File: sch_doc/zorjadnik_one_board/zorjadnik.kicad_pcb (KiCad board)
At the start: 2 copper layers, 63 parts, among them J1 OUT1, J10 output GND, J11 power supply GND, J12 spare port, J2 OUT2, J3 Vsb, J4 GND, J6 firmware, J7 cooling fan, J9 power supply Vout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

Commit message: собрал
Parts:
- moved R3 0.98 mm to (92.1, 46.1)
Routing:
- net GND: track 165.4 -> 167.3 mm
- net Net-(D5-Pad3): track 77.0 -> 75.7 mm
- net Net-(C7-Pad1): track 20.5 -> 21.5 mm
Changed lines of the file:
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@@
     (thickness 1.6)
     (drawings 0)
-    (tracks 480)
+    (tracks 483)
     (zones 0)
     (modules 63)
@@
   )
   (setup
-    (last_trace_width 1.5)
+    (last_trace_width 0.5)
     (user_trace_width 0.2)
     (user_trace_width 0.3)
@@
   )
   (module Resistor_SMD:R_0805_2012Metric (layer F.Cu)
-    (at 91.14536 46.14164 180)
+    (at 92.1258 46.09084 180)
     (descr "Resistor SMD 0805 (2012 Metric), square (rectangular) end terminal, IPC_7351 nominal, (Body size source: https://docs.google.com/spreadsheets/d/1BsfQQcO9C6DZCsRaXUlFlo91Tg2WpOkGARC1WS5S8t0/edit?usp=sharing), generated with kicad-footprint-generator")
     (tags resistor)
@@
     )
   )
+  (segment (start 107.07116 40.78732) (end 103.81488 40.78732) (width 0.5) (layer F.Cu) (net 1))
   (via (at 98.298 46.11624) (size 1.7) (drill 0.4) (layers F.Cu B.Cu) (net 1))
-  (segment (start 104.55148 47.91964) (end 104.55148 47.91456) (width 0.5) (layer B.Cu) (net 3))
-  (segment (start 104.55148 47.91456) (end 103.73868 47.10176) (width 0.5) (layer B.Cu) (net 3))
   (via (at 94.81566 55.36946) (size 1.7) (drill 0.4) (layers F.Cu B.Cu) (net 1))
   (segment (start 69.24358 67.9129) (end 69.22058 67.8899) (width 0.5) (layer F.Cu) (net 1))
@@
   (segment (start 78.99644 59.03468) (end 79.02956 59.00156) (width 0.5) (layer F.Cu) (net 1))
   (segment (start 79.02956 57.58698) (end 79.02448 57.5819) (width 0.5) (layer F.Cu) (net 1))
-  (segment (start 79.02956 59.00156) (end 79.02956 57.58698) (width 0.5) (layer F.Cu) (net 1))
   (segment (start 79.02956 59.00156) (end 80.129601 59.00156) (width 0.4) (layer F.Cu) (net 1))
   (segment (start 81.407561 59.364559) (end 82.057561 60.014559) (width 0.4) (layer F.Cu) (net 1))
@@
   (segment (start 107.25912 53.7778) (end 107.25912 54.06644) (width 0.5) (layer B.Cu) (net 2))
   (segment (start 107.54152 53.4954) (end 107.25912 53.7778) (width 0.5) (layer B.Cu) (net 2))
+  (segment (start 104.55148 47.91964) (end 104.55148 47.91456) (width 0.5) (layer B.Cu) (net 3))
+  (segment (start 104.55148 47.91456) (end 103.73868 47.10176) (width 0.5) (layer B.Cu) (net 3))
   (segment (start 104.50068 33.80232) (end 106.75112 33.80232) (width 0.3) (layer B.Cu) (net 3))
   (segment (start 104.12476 40.78732) (end 106.74096 40.78732) (width 0.5) (layer B.Cu) (net 3))
@@
   (segment (start 105.47604 44.391566) (end 105.361726 44.50588) (width 1.5) (layer F.Cu) (net 23))
   (segment (start 105.47604 42.6238) (end 105.47604 44.391566) (width 1.5) (layer F.Cu) (net 23))
-  (segment (start 92.26244 45.96206) (end 92.08286 46.14164) (width 0.5) (layer F.Cu) (net 23))
   (segment (start 73.52284 43.68692) (end 74.037 44.20108) (width 1.5) (layer F.Cu) (net 23))
   (segment (start 73.52284 43.01192) (end 73.52284 43.68692) (width 1.5) (layer F.Cu) (net 23))
   (segment (start 103.89876 44.20108) (end 104.089246 44.391566) (width 1.5) (layer F.Cu) (net 23))
   (segment (start 104.089246 44.391566) (end 105.47604 44.391566) (width 1.5) (layer F.Cu) (net 23))
-  (segment (start 92.08286 44.20338) (end 92.08286 46.14164) (width 0.5) (layer F.Cu) (net 23))
   (segment (start 92.08516 44.20108) (end 92.08286 44.20338) (width 0.5) (layer F.Cu) (net 23))
   (segment (start 74.037 44.20108) (end 92.08516 44.20108) (width 1.5) (layer F.Cu) (net 23))
@@
   (segment (start 95.75292 44.20108) (end 95.72244 44.23156) (width 0.5) (layer F.Cu) (net 23))
   (segment (start 95.75292 44.20108) (end 103.89876 44.20108) (width 1.5) (layer F.Cu) (net 23))
-  (segment (start 92.08516 44.20108) (end 95.75292 44.20108) (width 1.5) (layer F.Cu) (net 23))
-  (segment (start 92.30054 45.92396) (end 92.08286 46.14164) (width 0.5) (layer F.Cu) (net 23))
-  (segment (start 95.72244 45.92396) (end 92.30054 45.92396) (width 0.5) (layer F.Cu) (net 23))
+  (segment (start 95.55556 46.09084) (end 95.72244 45.92396) (width 0.5) (layer F.Cu) (net 23))
+  (segment (start 93.0633 46.09084) (end 95.55556 46.09084) (width 0.5) (layer F.Cu) (net 23))
+  (segment (start 93.0633 44.22926) (end 93.0633 46.09084) (width 0.5) (layer F.Cu) (net 23))
+  (segment (start 93.03512 44.20108) (end 93.0633 44.22926) (width 0.5) (layer F.Cu) (net 23))
+  (segment (start 93.03512 44.20108) (end 95.75292 44.20108) (width 1.5) (layer F.Cu) (net 23))
+  (segment (start 92.08516 44.20108) (end 93.03512 44.20108) (width 1.5) (layer F.Cu) (net 23))
   (segment (start 90.37856 58.67306) (end 91.89306 58.67306) (width 0.4) (layer F.Cu) (net 24) (status 10))
   (segment (start 92.04706 58.51906) (end 93.16456 58.51906) (width 0.4) (layer F.Cu) (net 24) (status 20))
@@
   (segment (start 90.20556 50.14976) (end 90.20556 49.385558) (width 0.4) (layer F.Cu) (net 24))
   (segment (start 90.20556 49.385558) (end 90.20556 48.6387) (width 0.5) (layer F.Cu) (net 24))
-  (segment (start 90.20786 48.6364) (end 90.20786 46.14164) (width 0.5) (layer F.Cu) (net 24))
   (segment (start 90.20556 48.6387) (end 90.20786 48.6364) (width 0.5) (layer F.Cu) (net 24))
   (segment (start 90.21064 54.77256) (end 90.21064 55.84952) (width 0.5) (layer F.Cu) (net 24))
@@
   (segment (start 89.08796 56.93156) (end 90.21064 55.84952) (width 0.3) (layer F.Cu) (net 24))
   (segment (start 90.21064 55.84952) (end 90.20556 55.81396) (width 0.3) (layer F.Cu) (net 24))
+  (segment (start 90.20556 48.6387) (end 90.20556 46.18736) (width 0.5) (layer F.Cu) (net 24))
+  (segment (start 90.30208 46.09084) (end 91.1883 46.09084) (width 0.5) (layer F.Cu) (net 24))
+  (segment (start 90.20556 46.18736) (end 90.30208 46.09084) (width 0.5) (layer F.Cu) (net 24))
   (segment (start 90.37856 58.02306) (end 91.40356 58.02306) (width 0.3) (layer F.Cu) (net 25) (status 10))
   (segment (start 91.765229 58.02306) (end 91.98356 57.804729) (width 0.3) (layer F.Cu) (net 25))

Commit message: полирнул меню, теперь есть функция выкючения
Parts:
- removed R14, R15: 100, Resistor_SMD:R_0805_2012Metric
- turned RV1 to 0 degrees
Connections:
- CB1 pad 2: Net-(CB1-Pad2) -> mode_but
- CB2 pad 2: Net-(CB2-Pad2) -> sel_but
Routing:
- net sel_but: track 42.6 -> 53.3 mm
- net mode_but: track 42.0 -> 52.7 mm
- net Net-(CB2-Pad2): track 8.81 -> 0.00 mm
- net Net-(CB1-Pad2): track 8.80 -> 0.00 mm

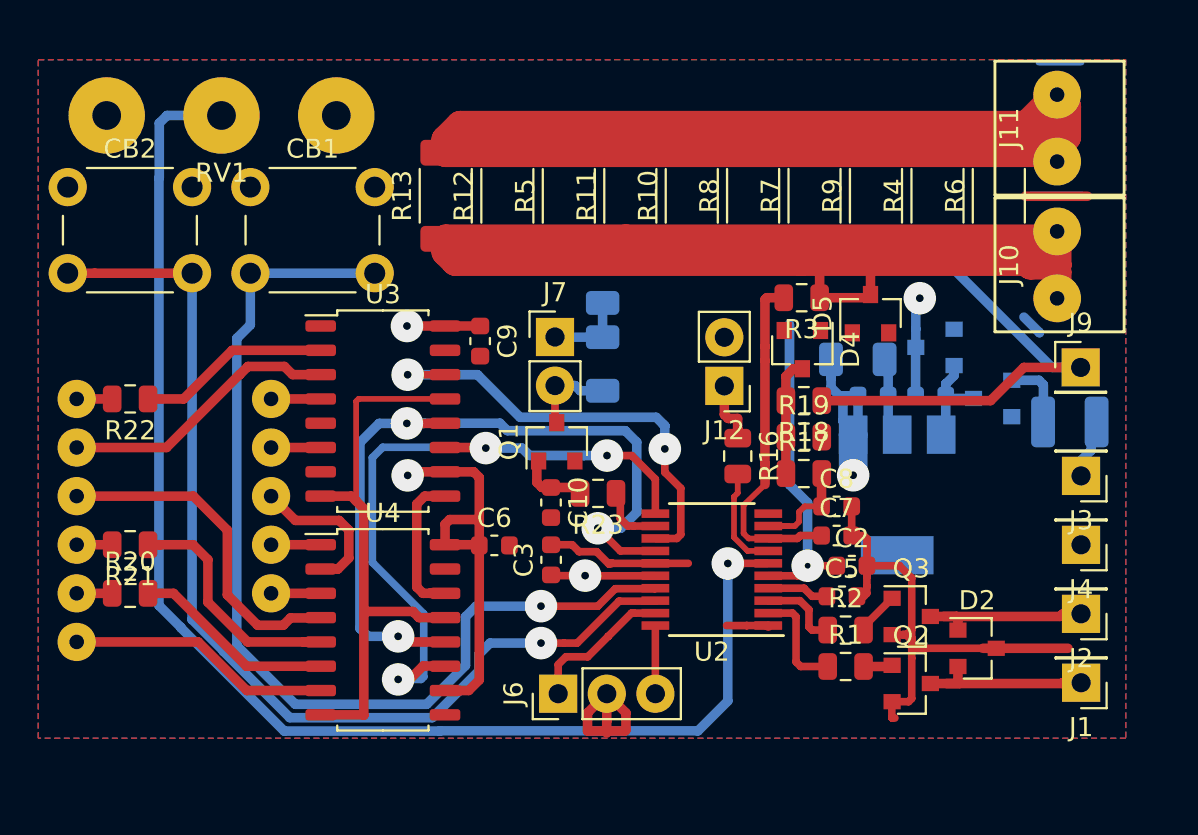
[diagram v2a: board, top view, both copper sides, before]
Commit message: список компонентов
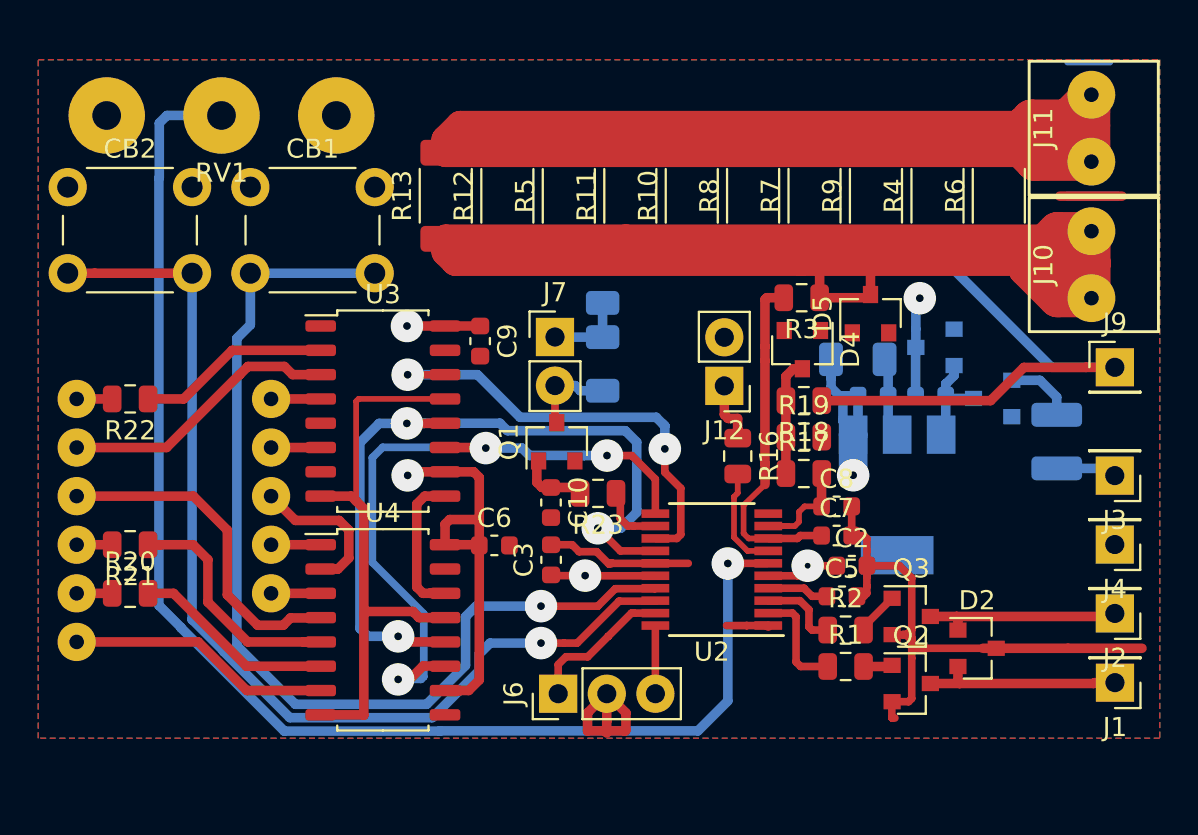
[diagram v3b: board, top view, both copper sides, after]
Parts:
- moved J10 1.79 mm to (107.3, 44.4)
- moved J11 1.79 mm to (107.3, 37.2)
- moved J9 1.79 mm to (108.5, 49.7)
- moved J2 1.77 mm to (108.5, 62.6)
- moved J1 1.77 mm to (108.5, 66.2)
- moved J3 1.76 mm to (108.5, 55.4)
- moved J4 1.76 mm to (108.5, 59.0)
- moved L1 1.23 mm to (105.5, 53.6), turned to 90 degrees
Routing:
- net +3V3: track 57.6 -> 43.4 mm
- net GND: track 167.3 -> 176.4 mm
- net Net-(D5-Pad3): track 75.7 -> 81.1 mm
- net +VDC: track 41.8 -> 45.4 mm
- net Net-(D2-Pad1): track 9.37 -> 10.4 mm
- net Net-(D2-Pad2): track 9.52 -> 10.6 mm
- net Net-(D3-Pad1): track 3.08 -> 3.64 mm

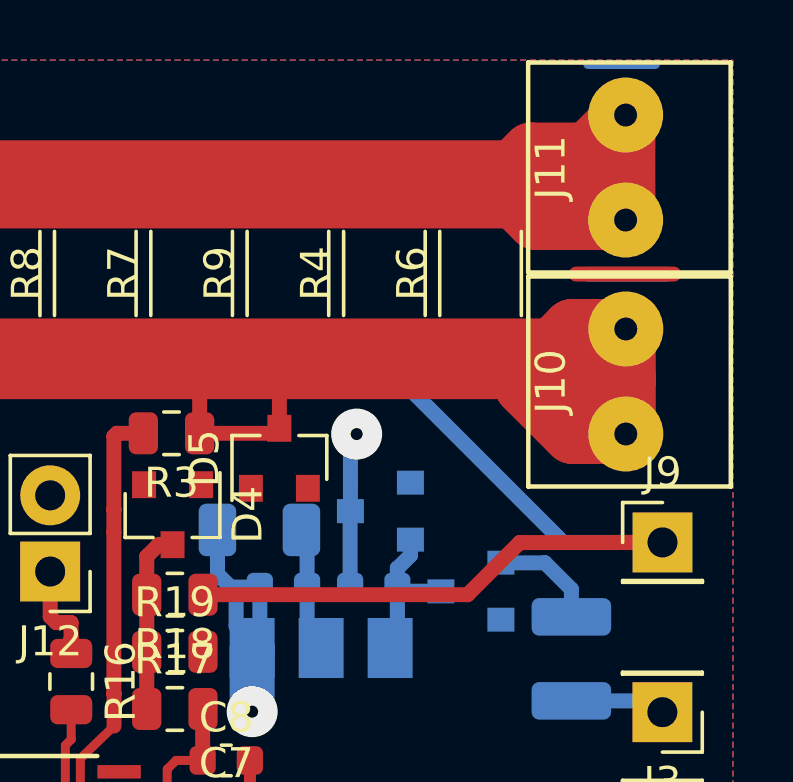
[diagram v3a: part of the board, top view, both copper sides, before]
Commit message: убрал сохранение настроек, не умею в такое
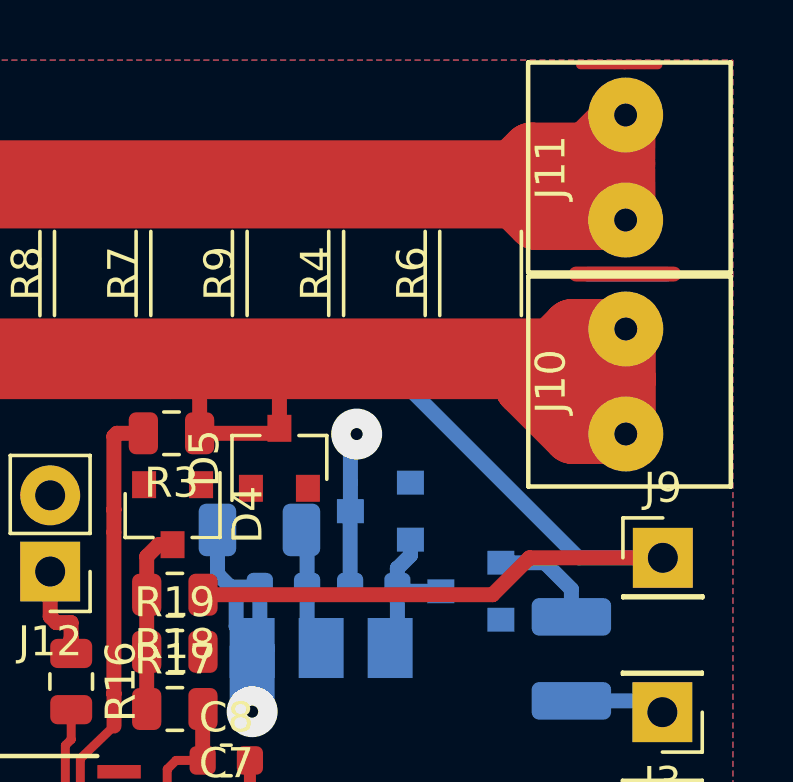
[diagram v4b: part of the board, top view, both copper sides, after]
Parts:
- moved J9 0.51 mm to (108.5, 50.2)
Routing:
- net GND: track 176.4 -> 179.0 mm
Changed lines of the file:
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@@
   )
   (setup
-    (last_trace_width 0.5)
+    (last_trace_width 0.25)
     (user_trace_width 0.2)
     (user_trace_width 0.3)
@@
       (hpglpenspeed 20)
       (hpglpendiameter 15.000000)
-      (psnegative true)
+      (psnegative false)
       (psa4output false)
       (plotreference false)
@@
   )
   (module Connector_PinHeader_2.54mm:PinHeader_1x01_P2.54mm_Vertical (layer F.Cu)
-    (at 108.49356 49.72812)
+    (at 108.50372 50.2412)
     (descr "Through hole straight pin header, 1x01, 2.54mm pitch, single row")
     (tags "Through hole pin header THT 1x01 2.54mm single row")
@@
     )
   )
+  (segment (start 105.76052 33.8074) (end 107.23372 33.8074) (width 0.3) (layer F.Cu) (net 1))
+  (segment (start 107.23372 33.8074) (end 108.34116 33.8074) (width 0.3) (layer F.Cu) (net 1))
   (segment (start 108.86948 40.78224) (end 105.6132 40.78224) (width 0.5) (layer F.Cu) (net 1))
   (via (at 98.298 46.11624) (size 1.7) (drill 0.4) (layers F.Cu B.Cu) (net 1))
@@
   (segment (start 56.09108 61.5399) (end 54.23458 61.5399) (width 0.5) (layer F.Cu) (net 6) (status 30))
   (segment (start 56.09108 58.9999) (end 54.23458 58.9999) (width 0.5) (layer F.Cu) (net 7) (status 30))
-  (segment (start 93.17506 51.47056) (end 101.99624 51.47056) (width 0.5) (layer F.Cu) (net 8))
-  (segment (start 101.99624 51.47056) (end 103.7336 49.7332) (width 0.5) (layer F.Cu) (net 8))
+  (segment (start 82.59696 43.56308) (end 81.72196 43.56308) (width 0.5) (layer B.Cu) (net 8))
+  (segment (start 99.03528 43.582) (end 99.03528 43.56308) (width 0.5) (layer B.Cu) (net 8))
   (segment (start 99.03528 43.56308) (end 82.59696 43.56308) (width 0.5) (layer B.Cu) (net 8))
-  (segment (start 82.59696 43.56308) (end 81.72196 43.56308) (width 0.5) (layer B.Cu) (net 8))
-  (segment (start 108.49356 49.72812) (end 105.1814 49.72812) (width 0.5) (layer B.Cu) (net 8))
-  (segment (start 99.03528 43.582) (end 99.03528 43.56308) (width 0.5) (layer B.Cu) (net 8))
-  (segment (start 105.1814 49.72812) (end 99.03528 43.582) (width 0.5) (layer B.Cu) (net 8))
-  (segment (start 106.98848 49.7332) (end 103.7336 49.7332) (width 0.5) (layer F.Cu) (net 8))
-  (segment (start 106.99356 49.72812) (end 106.98848 49.7332) (width 0.5) (layer F.Cu) (net 8))
-  (segment (start 108.49356 49.72812) (end 106.99356 49.72812) (width 0.5) (layer F.Cu) (net 8))
+  (segment (start 108.50372 50.2412) (end 105.69448 50.2412) (width 0.5) (layer B.Cu) (net 8))
+  (segment (start 105.69448 50.2412) (end 99.03528 43.582) (width 0.5) (layer B.Cu) (net 8))
+  (segment (start 104.05872 50.2412) (end 108.50372 50.2412) (width 0.5) (layer F.Cu) (net 8))
+  (segment (start 93.17506 51.47056) (end 102.82936 51.47056) (width 0.5) (layer F.Cu) (net 8))
+  (segment (start 102.82936 51.47056) (end 104.05872 50.2412) (width 0.5) (layer F.Cu) (net 8))
   (segment (start 92.07246 65.36436) (end 93.48446 65.36436) (width 0.4) (layer F.Cu) (net 9) (status 20))
   (segment (start 91.83116 65.12306) (end 92.07246 65.36436) (width 0.4) (layer F.Cu) (net 9))

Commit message: наладил, как сделаю трансформатор, так будет релиз
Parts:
- removed R10, R11, R12, R13, R9: 0.1R, Resistor_SMD:R_2010_5025Metric
- added R14: 1k, Resistor_SMD:R_0805_2012Metric, F.Cu at (89.9, 65.6)
- added R15: 1k, Resistor_SMD:R_0805_2012Metric, F.Cu at (88.0, 65.6)
- added REF**: MountingHole, MountingHole:MountingHole_2.1mm, F.Cu at (59.3, 70.5)
- D2: value D_x2_ACom_KKA -> BAT54
- D3: value D_x2_KCom_AAK -> BAV70
- D4, D5: value D_Zener_SOT23 -> D_Zener
- D6: value D_Zener -> PESD1CAN
- moved R5 5.34 mm to (85.3, 40.8)
- moved L1 3.83 mm to (103.1, 50.6), turned to 180 degrees
- moved R4 3.75 mm to (95.5, 40.8)
- moved R6 3.60 mm to (98.8, 40.8)
- moved D3 2.58 mm to (102.4, 53.9)
- moved J10 2.03 mm to (105.2, 44.4)
- moved J11 2.02 mm to (105.2, 37.2)
- moved R24 1.80 mm to (83.1, 46.1), turned to 180 degrees
- moved J1 1.49 mm to (107.0, 66.2)
- moved J2 1.49 mm to (107.0, 62.6)
- moved J3 1.49 mm to (107.0, 55.4)
- moved J4 1.49 mm to (107.0, 59.0)
- moved J9 1.49 mm to (107.0, 50.2)
- moved R8 0.87 mm to (88.7, 40.8)
- moved R7 0.71 mm to (92.1, 40.8)
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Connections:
- Q2 pad 1: Net-(Q2-Pad1) -> (no net)
- Q3 pad 1: Net-(Q3-Pad1) -> (no net)
- R1 pad 2: Net-(Q2-Pad1) -> (no net)
- R2 pad 2: Net-(Q3-Pad1) -> (no net)
- R23 pad 1: Net-(R23-Pad1) -> Net-(C10-Pad1)
- R23 pad 2: Net-(C10-Pad1) -> Net-(R23-Pad2)
- U2 pad 12: Net-(R23-Pad1) -> Net-(R23-Pad2)
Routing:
- net Net-(D5-Pad3): track 81.1 -> 57.3 mm
- net GND: track 179.0 -> 155.6 mm
- net Net-(R15-Pad1): track 4.27 -> 8.91 mm
- net +28V: track 3.19 -> 7.54 mm
- net +3V3: track 43.4 -> 47.4 mm, vias 4 -> 5
- net +VDC: track 45.4 -> 41.5 mm
- net (no net): track 0.00 -> 3.83 mm
- net Net-(R1-Pad1): track 5.65 -> 9.27 mm
- net Net-(R23-Pad2): track 0.00 -> 3.40 mm
- net Net-(R23-Pad1): track 3.40 -> 0.00 mm
- net Net-(Q3-Pad1): track 2.28 -> 0.00 mm
- net Net-(Q2-Pad1): track 1.55 -> 0.00 mm
- net Net-(D2-Pad1): track 10.4 -> 8.95 mm
- net Net-(D2-Pad2): track 10.6 -> 9.09 mm
- net Net-(C1-Pad1): track 5.41 -> 6.34 mm
